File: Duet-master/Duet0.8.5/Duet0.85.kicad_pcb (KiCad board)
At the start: 4 copper layers, 100 x 123 mm, 295 parts, among them J1 EXPANSION, J10 E0 MOT/STOP, J11 E0 HEAT, J12 E0 TEMP, J13 E1 HEAT, J14 E1 TEMP, J15 uSDHC, J16 Z VREF, J17 Y VREF, J18 E0 VREF, J19 ETHERNET, J2 E1 VREF, J20 5V_PS, J21 JTAG, J22 USB, J23 POWER IN, J24 GND V_IN, J25 FAN 0 +, J26 GND, J27 GND, J28 Probe, J29 FAN 1 +, J3 X VREF, J30 PanelDUE, J31 GND V_IN, J4 BED HEAT, J5 BED TEMP, J6 E1 MOT/STOP, J7 Z MOT/STOP, J8 Y MOT/STOP, J9 X MOT/STOP, U1 ATSAM3X8E, U11 A4982SLPTR, U2 TC2117-3.3VDBTR, U3 A4403, U4 KSZ8051RNL, U5 A4982SLPTR, U6 A4982SLPTR, U7 A4982SLPTR, U8 A4982SLPTR, U9 MCP44X1, X1 CRYSTAL_4PIN, X2 CRYSTAL_4PIN

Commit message: PCB layout of components started
Experienced advice welcome.
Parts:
- removed ?: , Fixing_M4
- removed ? (x3): , Fixing_M3
- removed ?: , Duet_logo_text_conv
- removed C100, C104: 0u22, C_0603
- removed C101, C103, C105, C110, C111, C112, C93: 0u1, C_0603
- removed C102, C113, C94, C99: 100u, C_ELEC_6.3x7.7
- removed C95: 1u, C_0603
- removed C96: 22nF, C_0603
- removed C97, C98: 10u, C_0805
- removed Fid (x4): VAL**, Fiducial
- removed the J19 at (164.5, 148.4)
- removed J25: FAN 0 +, PIN_ARRAY_2X1
- removed J26, J27: GND, TP
- removed J28: Probe, PIN_ARRAY_4x1
- removed J29: FAN 1 +, PIN_ARRAY_2X1
- removed J30: PanelDUE, PIN_ARRAY_4x1
- removed J31: GND V_IN, PIN_ARRAY_2X1
- removed the J9 at (83.4, 92.1)
- removed JP10: ATX_5V_EN, JUMPER
- removed JP9: 5V_EN, JUMPER
- added C54: 10u, Melter_Connections:10mf_capacitor, F.Cu at (165.2, 70.5)
- added C6: 100u, Melter_Connections:100mf_capacitor, F.Cu at (257.4, 106.4)
- added C63: 10u, Melter_Connections:10mf_capacitor, F.Cu at (47.9, 108.5)
- added C73: 4u7, Melter_Connections:4uf7_capacitor, F.Cu at (214.4, 150.4)
- added C74: 0u1, Melter_Connections:0mf1_capacitor, F.Cu at (214.2, 148.7)
- added C79: 0u1, Melter_Connections:0mf1_capacitor, F.Cu at (217.9, 159.6)
- added C80: 10p, Melter_Connections:10pf_capacitor, F.Cu at (225.3, 159.0)
- added C81: 0u1, Melter_Connections:0mf1_capacitor, F.Cu at (217.9, 161.1)
- added C82: 0u1, Melter_Connections:0mf1_capacitor, F.Cu at (217.9, 162.6)
- added C83: 4u7, Melter_Connections:4uf7_capacitor, F.Cu at (216.8, 133.8)
- added C84: 0u1, Melter_Connections:0mf1_capacitor, F.Cu at (217.0, 132.0)
- added C85: 4u7, Melter_Connections:4uf7_capacitor, F.Cu at (223.6, 139.2)
- added C86: 0u1, Melter_Connections:0mf1_capacitor, F.Cu at (223.6, 141.0)
- added C87: 0u1, Melter_Connections:0mf1_capacitor, F.Cu at (223.6, 137.4)
- added C88: 10nF, Melter_Connections:10nf_capacitor, F.Cu at (223.6, 135.8)
- added C89: 0u1, Melter_Connections:0mf1_capacitor, F.Cu at (223.6, 134.2)
- added D22: LED0_R, Melter_Connections:LED0_diode, F.Cu at (174.4, 119.5)
- added D23: LED1_R, Melter_Connections:LED0_diode, F.Cu at (157.2, 119.9)
- added D24: LED0_B, Melter_Connections:LED0_diode, F.Cu at (174.4, 121.1)
- added D25: LED1_B, Melter_Connections:LED0_diode, F.Cu at (157.2, 121.5)
- added D26: FAN0, Melter_Connections:FAN0_diode, F.Cu at (95.8, 122.7)
- added D27: FAN1, Melter_Connections:FAN1_diode, F.Cu at (108.5, 118.8)
- added J19: USB, Melter_Connections:mUSB_new, F.Cu at (113.8, 66.5)
- added J19: USB_B, Melter_Connections:USB_Bsmd, F.Cu at (115.7, 74.9)
- added J9: 5V_PS, Melter_Connections:5VPSGND_PIN_ARRAY_3X1, F.Cu at (140.8, 134.4)
- added J9: 5V_PS, Melter_Connections:5VPSGND_PIN_ARRAY_3X1, F.Cu at (132.4, 124.6)
- added JP1: 5V_EN, Melter_Connections:JUMPER, F.Cu at (132.4, 112.4)
- added JP2: ATX_5V_EN, Melter_Connections:JUMPER, F.Cu at (132.4, 103.1)
- added K1: LED STRIP 1, Melter_Connections:USB_2, F.Cu at (173.5, 114.8)
- added K2: LED STRIP 2, Melter_Connections:USB_2, F.Cu at (156.5, 114.8)
- added K3: SENSE 1, Melter_Connections:USB_2, F.Cu at (73.5, 114.8)
- added K4: SENSE 2, Melter_Connections:USB_2, F.Cu at (56.5, 114.8)
- added R101: 4k7, Melter_Connections:4k7_R_0603, F.Cu at (108.5, 122.0)
- added R102: 100k, Melter_Connections:100k_R_0603, F.Cu at (239.2, 133.8)
- added R103: 6k8, Melter_Connections:6k8_R_0603, F.Cu at (225.3, 160.8)
- added R104: 100k, Melter_Connections:100k_R_0603, F.Cu at (232.8, 133.4)
- added R105: 100k, Melter_Connections:100k_R_0603, F.Cu at (236.0, 133.6)
- added R106: 10K, Melter_Connections:10k_R_0603, F.Cu at (235.8, 137.2)
- added R107: 10K, Melter_Connections:10k_R_0603, F.Cu at (239.0, 137.2)
- added R108: 10K, Melter_Connections:10k_R_0603, F.Cu at (233.2, 140.2)
- added R109: 10K, Melter_Connections:10k_R_0603, F.Cu at (232.8, 137.0)
- added R83: 4k7, Melter_Connections:4k7_R_0603, F.Cu at (141.1, 66.6)
- added TR10: PMV40UN2, Melter_Connections:PMV40UN2_SOT-23, F.Cu at (181.5, 109.0)
- added TR11: PMV40UN2, Melter_Connections:PMV40UN2_SOT-23, F.Cu at (165.9, 109.0)
- added TR12: PMV40UN2, Melter_Connections:PMV40UN2_SOT-23, F.Cu at (95.0, 107.3)
- added TR13: PMV40UN2, Melter_Connections:PMV40UN2_SOT-23, F.Cu at (112.3, 108.2)
- added U10: POWER/SENSE 2, Melter_Connections:USB_3, F.Cu at (107.5, 114.2)
- added U12: ATSAM3X8E, Melter_Connections:LQFP144, F.Cu at (140.2, 84.9)
- C1: value 2u2 -> 0u22; footprint C_0603 -> Melter_Connections:0mf22_capacitor
- C10: value 22u -> 0u22; footprint C_1210 -> Melter_Connections:0mf22_capacitor
- C11: value 22u -> 0u1; footprint C_1210 -> Melter_Connections:0mf1_capacitor
- C12: value 2u2 -> 0u1; footprint C_0805 -> Melter_Connections:0mf1_capacitor
- C13: value 1u -> 0u1; footprint C_0603 -> Melter_Connections:0mf1_capacitor
- C14, C17, C25, C28, C34, C35, C38, C39, C40, C41, C42, C46, C60, C64, C70, C72, C75, C78: footprint C_0603 -> Melter_Connections:0mf1_capacitor
- C15, C16, C24, C29: value 0u1 -> 0u22; footprint C_0603 -> Melter_Connections:0mf22_capacitor
- C18, C4, C7: value 10u -> 0u1; footprint C_0805 -> Melter_Connections:0mf1_capacitor
- C19: value 10u -> 100u; footprint C_0805 -> Melter_Connections:100mf_capacitor
- C2: value 0u01 -> 0u22; footprint C_0603 -> Melter_Connections:0mf22_capacitor
- C20, C31: value 0u22 -> 100u; footprint C_0603 -> Melter_Connections:100mf_capacitor
- C21, C26, C27, C30, C36, C37: value 0u22 -> 0u1; footprint C_0603 -> Melter_Connections:0mf1_capacitor
- C22, C3, C32: value 100u -> 0u1; footprint C_ELEC_6.3x7.7 -> Melter_Connections:0mf1_capacitor
- C23, C33: value 100u -> 0u22; footprint C_ELEC_6.3x7.7 -> Melter_Connections:0mf22_capacitor
- C43, C52: value 0u1 -> 1u; footprint C_0603 -> Melter_Connections:1mf_capacitor
- C44: value 10p -> 2u2; footprint C_0603 -> Melter_Connections:2mf2_capacitor
- C45: value 10p -> 100u; footprint C_0603 -> Melter_Connections:100mf_capacitor
- C47: footprint C_0805 -> Melter_Connections:10mf_capacitor
- C48: value 0u1 -> 22nF; footprint C_0603 -> Melter_Connections:22nf_capacitor
- C49, C50, C62, C69: value 0u1 -> 10u; footprint C_0603 -> Melter_Connections:10mf_capacitor
- C5, C51, C67: value 0u1 -> 100u; footprint C_0603 -> Melter_Connections:100mf_capacitor
- C53: value 10u -> 2u2; footprint C_0805 -> Melter_Connections:2mf2_capacitor
- C55, C56: value 0u1 -> 22p; footprint C_0603 -> Melter_Connections:22pf_capacitor
- C57: value 0u1 -> 22u; footprint C_0603 -> Melter_Connections:22mf_Capacitor_1210
- C58: value 2u2 -> 22u; footprint C_0805 -> Melter_Connections:22mf_Capacitor_1210
- C59: value 4u7 -> 2u2; footprint C_0805 -> Melter_Connections:2mf2_capacitor
- C61: value 4u7 -> 0u1; footprint C_0805 -> Melter_Connections:0mf1_capacitor
- C65: value 10p -> 0u1; footprint C_0603 -> Melter_Connections:0mf1_capacitor
- C66: value 4u7 -> 100u; footprint C_0805 -> Melter_Connections:100mf_capacitor
- C68: value 4u7 -> 10u; footprint C_0805 -> Melter_Connections:10mf_capacitor
- C71: value 0u1 -> 4u7; footprint C_0603 -> Melter_Connections:4uf7_capacitor
- C76, C77: value 0u1 -> 10p; footprint C_0603 -> Melter_Connections:10pf_capacitor
- C8: value 22p -> 0u1; footprint C_0603 -> Melter_Connections:0mf1_capacitor
- C9: value 22p -> 0u22; footprint C_0603 -> Melter_Connections:0mf22_capacitor
- C90: value 10nF -> 0u1; footprint C_0603 -> Melter_Connections:0mf1_capacitor
- C91: value 0.1u -> 0u1; footprint C_0603 -> Melter_Connections:0mf1_capacitor
- C92: value 100u -> 0u01; footprint C_ELEC_6.3x7.7 -> Melter_Connections:0mf01_Capacitor
- D1: value SS3P4 -> 1SS400T1G; footprint DO-220AA -> Melter_Connections:1SS400T1G
- D10: value Z Stop -> VIN; footprint D_0603 -> Melter_Connections:V_IN_Diode_0603
- D11: value E0 Stop -> 5V+; footprint D_0603 -> Melter_Connections:5V_Diode_0603
- D12: value X Stop -> 3.3V; footprint D_0603 -> Melter_Connections:33V_Diode_0603
- D13, D14: footprint uSMA -> Melter_Connections:SS14M
- D15: value VIN -> USB; footprint D_0603 -> Melter_Connections:USB_Diode_0603
- D16: value 3.3V -> TS4148; footprint D_0603 -> Melter_Connections:TS4148_Diode_0805
- D17: value 5V+ -> TS4148; footprint D_0603 -> Melter_Connections:TS4148_Diode_0805
- D18: value 1SS400T1G -> Bed Heat; footprint SOD-523 -> Melter_Connections:BED_Diode_0603
- D19: value E1 Stop -> E0 Heat; footprint D_0603 -> Melter_Connections:E0_Diode_0603
- D2: value SS3P4 -> E1 Stop; footprint DO-220AA -> Melter_Connections:E1STOP_diode
- D20: value E1 Heat -> LED0_G; footprint D_0603 -> Melter_Connections:LED0_diode
- D21: value FAN1 -> LED1_G; footprint D_0603 -> Melter_Connections:LED0_diode
- D3: value USB -> Y Stop; footprint D_0603 -> Melter_Connections:YSTOP_diode
- D4: value TS4148 -> Z Stop; footprint D_0805 -> Melter_Connections:ZSTOP_diode
- D5: value TS4148 -> E2 Stop; footprint D_0805 -> Melter_Connections:E2STOP_diode
- D6: value Bed Heat -> E0 Stop; footprint D_0603 -> Melter_Connections:E0STOP_diode
- D7: value E0 Heat -> X Stop; footprint D_0603 -> Melter_Connections:XSTOP_diode
- D8: value FAN0 -> SS3P4; footprint D_0603 -> Melter_Connections:SS3P4
- D9: value Y Stop -> SS3P4; footprint D_0603 -> Melter_Connections:SS3P4
- J1: value EXPANSION -> X VREF; footprint PIN_ARRAY_25X2 -> Melter_Connections:Vref
- J10: value E0 MOT/STOP -> GND V_IN; footprint PIN_ARRAY_7X1 -> Melter_Connections:JUMPER
- J11: value E0 HEAT -> GND V_IN; footprint PIN_ARRAY_2X1 -> Melter_Connections:JUMPER
- J12: value E0 TEMP -> E1 TEMP; footprint PIN_ARRAY_2X1 -> Melter_Connections:PIN_ARRAY_2X1
- J13: value E1 HEAT -> Probe; footprint PIN_ARRAY_2X1 -> Melter_Connections:PIN_ARRAY_4x1
- J14: value E1 TEMP -> Z STEPPER MOTOR; footprint PIN_ARRAY_2X1 -> Melter_Connections:USB_2
- J15: value uSDHC -> Y STEPPER MOTOR; footprint uSD_SKT -> Melter_Connections:USB_2
- J16: value Z VREF -> X STEPPER MOTOR; footprint Vref -> Melter_Connections:USB_2
- J17: value Y VREF -> E0 STEPPER MOTOR; footprint Vref -> Melter_Connections:USB_2
- J18: value E0 VREF -> E1 STEPPER MOTOR; footprint Vref -> Melter_Connections:USB_2
- J2: value E1 VREF -> Z VREF; footprint Vref -> Melter_Connections:Vref
- J20: value 5V_PS -> uSDHC; footprint PIN_ARRAY_3X1 -> Melter_Connections:SD_Card_Receptacle; moved to B.Cu
- J21: value JTAG -> ETHERNET; footprint MICRO_5x2 -> Melter_Connections:RJ45_MAG
- J22: value USB -> GND; footprint uUSB_new -> Melter_Connections:GND_TP
- J23: value POWER IN -> JTAG; footprint TERM_2-WAY_6.35mm -> Melter_Connections:PIN_ARRAY_5x2
- J24: value GND V_IN -> GND; footprint PIN_ARRAY_2X1 -> Melter_Connections:GND_TP
- J3: value X VREF -> Y VREF; footprint Vref -> Melter_Connections:Vref
- J4: value BED HEAT -> E0 VREF; footprint TERM_2-WAY_6.35mm -> Melter_Connections:Vref
- J5: value BED TEMP -> E1 VREF; footprint PIN_ARRAY_2X1 -> Melter_Connections:Vref
- J6: value E1 MOT/STOP -> EXPANSION; footprint PIN_ARRAY_7X1 -> Melter_Connections:PIN_ARRAY_25X2
- J7: value Z MOT/STOP -> PanelDUE; footprint PIN_ARRAY_7X1 -> Melter_Connections:PIN_ARRAY_4x1
- J8: value Y MOT/STOP -> POWER IN; footprint PIN_ARRAY_7X1 -> Melter_Connections:V_TERM_2-WAY_6.35mm
- L1: footprint L_6x6 -> Melter_Connections:10mH_L_6x6
- L2: footprint R_0603 -> Melter_Connections:FERRITE_BEAD
- L3, L4, L5, L6, L7: footprint R_0603 -> Melter_Connections:100Mhz_R_0603
- R1: value 3K3 -> 100k; footprint R_0603 -> Melter_Connections:100k_R_0603
- R10, R7, R8, R9: value 33R -> 0R1; footprint R_0603 -> Melter_Connections:0R1_R_1206
- R100: footprint R_0603 -> Melter_Connections:4k7_R_0603
- R11, R13: value 1k -> 100k; footprint R_0603 -> Melter_Connections:100k_R_0603
- R12, R14, R67: value 4k7 -> 10k; footprint R_0603 -> Melter_Connections:10k_R_0603
- R15: value 6k49 1% -> 0R; footprint R_0603 -> Melter_Connections:0R_R_0603
- R16: value 220R -> 0R; footprint R_0603 -> Melter_Connections:0R_R_0603
- R17, R20: value 220R -> 0R1; footprint R_0603 -> Melter_Connections:0R1_R_1206
- R18: value 470R -> 0R1; footprint R_0603 -> Melter_Connections:0R1_R_1206
- R19: value 4K7 -> 0R1; footprint R_0603 -> Melter_Connections:0R1_R_1206
- R2: value 39R 1% -> 10k; footprint R_0603 -> Melter_Connections:10k_R_0603
- R21: value 4K7 -> 4k7; footprint R_0603 -> Melter_Connections:4k7_R_0603
- R22: value 470R -> 100k; footprint R_0603 -> Melter_Connections:100k_R_0603
- R23: value 220R -> 10k; footprint R_0603 -> Melter_Connections:10k_R_0603
- R24, R82: value 10K -> 4k7; footprint R_0603 -> Melter_Connections:4k7_R_0603
- R25: value 100k -> 0R; footprint R_0603 -> Melter_Connections:0R_R_0603
- R26: value 100k -> 2k7; footprint R_0603 -> Melter_Connections:2k7_R_0603
- R27: value 10k -> 2K15; footprint R_0603 -> Melter_Connections:2k15_R_0603
- R28: value 100k -> 0R1; footprint R_0603 -> Melter_Connections:0R1_R_1206
- R29: value 10k -> 0R1; footprint R_0603 -> Melter_Connections:0R1_R_1206
- R3: value 39R 1% -> 100k; footprint R_0603 -> Melter_Connections:100k_R_0603
- R30: value 0R -> 10k; footprint R_0603 -> Melter_Connections:10k_R_0603
- R31: value 0R -> 100R; footprint R_0603 -> Melter_Connections:100k_R_0603
- R32, R33: value 0R1 -> 100R; footprint R_1206 -> Melter_Connections:100R_R_0603
- R34, R35: value 0R1 -> 680R; footprint R_1206 -> Melter_Connections:680R_R_0603
- R36, R40: value 100k -> 680R; footprint R_0603 -> Melter_Connections:680R_R_0603
- R37: value 2k7 -> 100R; footprint R_0603 -> Melter_Connections:100R_R_0603
- R38: value 100k -> 100R; footprint R_0603 -> Melter_Connections:100R_R_0603
- R39: value 10k -> 100R; footprint R_0603 -> Melter_Connections:100R_R_0603
- R4, R99: footprint R_0603 -> Melter_Connections:10k_R_0603
- R41: value 10k -> 680R; footprint R_0603 -> Melter_Connections:680R_R_0603
- R42: value 0R -> 680R; footprint R_0603 -> Melter_Connections:680R_R_0603
- R43: value 0R -> 100K; footprint R_0603 -> Melter_Connections:100k_R_0603
- R44, R45: footprint R_1206 -> Melter_Connections:0R1_R_1206
- R46: value 0R1 -> 2k7; footprint R_1206 -> Melter_Connections:2k7_R_0603
- R47, R93: value 0R1 -> 4k7; footprint R_1206 -> Melter_Connections:4k7_R_0603
- R48: value 6k8 -> 2K15; footprint R_0603 -> Melter_Connections:2k15_R_0603
- R49: value 100k -> 3K92; footprint R_0603 -> Melter_Connections:3k92_R_0603
- R5: value 10k -> 0R; footprint R_0603 -> Melter_Connections:0R_R_0603
- R50: value 4k7 -> 750R; footprint R_0603 -> Melter_Connections:750R_R_0603
- R51: value 4k7 -> 470R; footprint R_0603 -> Melter_Connections:470R_R_0603
- R52: value 100k -> 10K; footprint R_0603 -> Melter_Connections:10k_R_0603
- R53: value 4K7 -> 10K; footprint R_0603 -> Melter_Connections:10k_R_0603
- R54: value 2k7 -> 39R 1%; footprint R_0603 -> Melter_Connections:39_1per_R_0603
- R55: value 4k7 -> 39R 1%; footprint R_0603 -> Melter_Connections:39_1per_R_0603
- R56, R57, R59: value 100R -> 47K; footprint R_0603 -> Melter_Connections:47k_R_0603
- R58: value 100R -> 3K3; footprint R_0603 -> Melter_Connections:3k3_R_0603
- R6: value 33R -> 0R; footprint R_0603 -> Melter_Connections:0R_R_0603
- R60: value 470R -> 47K; footprint R_0603 -> Melter_Connections:47k_R_0603
- R61: value 2K15 -> 10k; footprint R_0603 -> Melter_Connections:10k_R_0603
- R62, R63, R64: value 10K -> 33R; footprint R_0603 -> Melter_Connections:33R_R_0603
- R65: value 4k7 -> 33R; footprint R_0603 -> Melter_Connections:33R_R_0603
- R66: value 10k -> 33R; footprint R_0603 -> Melter_Connections:33R_R_0603
- R68: value 4k7 -> 1k; footprint R_0603 -> Melter_Connections:1k_R_0603
- R69, R71, R96: value 680R -> 4k7; footprint R_0603 -> Melter_Connections:4k7_R_0603
- R70: value 680R -> 1k; footprint R_0603 -> Melter_Connections:1k_R_0603
- R72: value 680R -> 6k49 1%; footprint R_0603 -> Melter_Connections:6k49_1_per_R_0603
- R73, R74: value 47K -> 220R; footprint R_0603 -> Melter_Connections:220R_R_0603
- R75, R76: value 47K -> 100k; footprint R_0603 -> Melter_Connections:100k_R_0603
- R77, R78: value 100k -> 470R; footprint R_0603 -> Melter_Connections:470R_R_0603
- R79: value 470R -> 4K7; footprint R_0603 -> Melter_Connections:4k7_R_0603
- R80, R81: value 10K -> 220R; footprint R_0603 -> Melter_Connections:220R_R_0603
- R84: value 100K -> 4K7; footprint R_0603 -> Melter_Connections:4k7_R_0603
- R85: value 0R1 -> 4K7; footprint R_1206 -> Melter_Connections:4k7_R_0603
- R86, R94: value 0R1 -> 10K; footprint R_1206 -> Melter_Connections:10k_R_0603
- R87: value 3K92 -> 10K; footprint R_0603 -> Melter_Connections:10k_R_0603
- R88: value 750R -> 4k7; footprint R_0603 -> Melter_Connections:4k7_R_0603
- R89: value 100k -> 4k7; footprint R_0603 -> Melter_Connections:4k7_R_0603
- R90: value 10k -> 10K; footprint R_0603 -> Melter_Connections:10k_R_0603
- R91: value 0R -> 10K; footprint R_0603 -> Melter_Connections:10k_R_0603
- R92: value 2K15 -> 4k7; footprint R_0603 -> Melter_Connections:4k7_R_0603
- R95: value 100R -> 10K; footprint R_0603 -> Melter_Connections:10k_R_0603
- R97: value 220R -> 4k7; footprint R_0603 -> Melter_Connections:4k7_R_0603
- R98: value 4k7 -> 10K; footprint R_0603 -> Melter_Connections:10k_R_0603
- S1: value RESET -> ERASE; footprint SW_SIDE_1 -> Melter_Connections:SW_SIDE_1
- S2: value ERASE -> RESET; footprint SW_SIDE_1 -> Melter_Connections:SW_SIDE_1
- SJ1, SJ10, SJ4, SJ5, SJ8, SJ9: footprint SJ -> Melter_Connections:SJump
- SJ2, SJ6: value MS1 -> MS2; footprint SJ -> Melter_Connections:SJump
- SJ3, SJ7: value MS2 -> MS1; footprint SJ -> Melter_Connections:SJump
- TR1, TR3: footprint SOT-23 -> Melter_Connections:BSH105_SOT-23
- TR2: value IPD036N04L -> BSH105; footprint D-PAK -> Melter_Connections:BSH105_SOT-23
- TR4: footprint D-PAK -> Melter_Connections:IPD036N04L_D-PAK
- TR5: value PMV40UN2 -> IPD036N04L; footprint SOT-23 -> Melter_Connections:IPD036N04L_D-PAK
- TR6, TR7: value BSH105 -> PMV40UN2; footprint SOT-23 -> Melter_Connections:PMV40UN2_SOT-23
- TR8: value IPD036N04L -> PMV40UN2; footprint D-PAK -> Melter_Connections:PMV40UN2_SOT-23
- TR9: footprint SOT-23 -> Melter_Connections:PMV40UN2_SOT-23
- U1: value ATSAM3X8E -> A4982SLPTR; footprint LQFP144 -> Melter_Connections:A4982SPLTR_TSSOP-24-thin_pads
- U11: value A4982SLPTR -> KSZ8051RNL; footprint TSSOP-24-thin_pads -> Melter_Connections:KSZ8051RNL
- U2: value TC2117-3.3VDBTR -> A4982SLPTR; footprint SOT-223 -> Melter_Connections:A4982SPLTR_TSSOP-24-thin_pads
- U3: value A4403 -> A4982SLPTR; footprint QFN16-4x4 -> Melter_Connections:A4982SPLTR_TSSOP-24-thin_pads
- U4: value KSZ8051RNL -> A4982SLPTR; footprint QFN32-5x5 -> Melter_Connections:A4982SPLTR_TSSOP-24-thin_pads
- U5: footprint TSSOP-24-thin_pads -> Melter_Connections:A4982SPLTR_TSSOP-24-thin_pads
- U6: value A4982SLPTR -> MCP44X1; footprint TSSOP-24-thin_pads -> Melter_Connections:MCP44X1_TSSOP-20
- U7: value A4982SLPTR -> TC2117-3.3VDBTR; footprint TSSOP-24-thin_pads -> Melter_Connections:TC2117-3.3VDBTR
- U8: value A4982SLPTR -> A4403; footprint TSSOP-24-thin_pads -> Melter_Connections:A4403_QFN16-4x4
- U9: value MCP44X1 -> POWER/SENSE 1; footprint TSSOP-20 -> Melter_Connections:USB_3
- X1, X2: footprint Xtal_5x3.2 -> Melter_Connections:Xtal_5x3.2
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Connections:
- C1 pad 1: N-000009 -> Net-(C1-Pad1)
- C10 pad 1: N-00000252 -> +3.3V
- C11 pad 1: +3.3V -> Net-(C11-Pad1)
- C11 pad 2: GND -> Net-(C11-Pad2)
- C12 pad 1: N-00000264 -> Net-(C12-Pad1)
- C12 pad 2: GND -> Net-(C12-Pad2)
- C13 pad 1: VBUS -> X_REF
- C14 pad 1: X_REF -> Z_REF
- C15 pad 1: Z_REF -> Net-(C15-Pad1)
- C16 pad 1: N-00000247 -> Net-(C16-Pad1)
- C17 pad 1: N-00000262 -> GND
- C17 pad 2: GND -> V_IN
- C18 pad 1: E0_THERMISTOR -> GND
- C18 pad 2: VSSA -> V_IN
- C19 pad 1: BED_THERMISTOR -> V_IN
- C19 pad 2: VSSA -> GND
- C2 pad 1: +3.3V -> Net-(C2-Pad1)
- C2 pad 2: RESET -> GND
- C20 pad 1: N-00000191 -> V_IN
- C21 pad 1: N-00000169 -> Net-(C21-Pad1)
- C21 pad 2: GND -> V_IN
- C22 pad 1: V_IN -> Net-(C22-Pad1)
- C22 pad 2: GND -> V_IN
- C23 pad 1: V_IN -> +3.3V
- C24 pad 1: N-00000186 -> +3.3V
- C24 pad 2: V_IN -> GND
- C25 pad 1: N-00000172 -> Net-(C25-Pad1)
- C25 pad 2: V_IN -> Net-(C25-Pad2)
- C26 pad 1: +3.3V -> Net-(C26-Pad1)
- C26 pad 2: GND -> Net-(C26-Pad2)
- C27 pad 1: +3.3V -> Y_REF
- C28 pad 1: N-00000195 -> E0_REF
- C28 pad 2: N-00000190 -> GND
- C29 pad 1: N-00000196 -> Net-(C29-Pad1)
- C29 pad 2: N-00000163 -> GND
- C3 pad 1: N-000009 -> GND
- C3 pad 2: GND -> V_IN
- C30 pad 1: N-00000213 -> GND
- C30 pad 2: GND -> V_IN
- C31 pad 1: N-00000208 -> V_IN
- C32 pad 1: V_IN -> Net-(C32-Pad1)
- C32 pad 2: GND -> V_IN
- C33 pad 1: V_IN -> +3.3V
- C34 pad 1: N-00000215 -> Net-(C34-Pad1)
- C34 pad 2: V_IN -> Net-(C34-Pad2)
- C35 pad 1: N-00000209 -> +3.3V
- C35 pad 2: V_IN -> GND
- C36 pad 1: +3.3V -> E1_REF
- C37 pad 1: +3.3V -> Y_STOP
- C38 pad 1: N-00000194 -> Z_STOP
- C38 pad 2: N-00000180 -> GND
- C39 pad 1: N-00000178 -> E1_STOP
- C39 pad 2: N-00000193 -> GND
- C4 pad 1: +3.3V -> GND
- C4 pad 2: GND -> V_IN
- C40 pad 1: X_STOP -> E2_STOP
- C41 pad 1: Y_STOP -> X_STOP
- C42 pad 1: Z_STOP -> E0_STOP
- C43 pad 1: E0_STOP -> +5V
- C44 pad 1: N-0000039 -> Net-(C44-Pad1)
- C45 pad 1: N-0000026 -> Net-(C44-Pad1)
- C46 pad 1: +3.3V -> Net-(C46-Pad1)
- C48 pad 1: +3.3V -> Net-(C48-Pad1)
- C48 pad 2: GND -> Net-(C48-Pad2)
- C49 pad 1: +3.3V -> +5V
- C5 pad 1: N-000003 -> V_IN
- C50 pad 1: +3.3V -> +5V
- C51 pad 1: +3.3V -> +5V
- C52 pad 1: /Processor/VDDCORE -> VBUS
- C53 pad 1: E1_THERMISTOR -> +3.3V
- C53 pad 2: VSSA -> GND
- C55 pad 1: +3.3V -> GND
- C55 pad 2: GND -> Net-(C55-Pad2)
- C56 pad 1: Y_REF -> GND
- C56 pad 2: GND -> Net-(C56-Pad2)
- C57 pad 1: E0_REF -> Net-(C57-Pad1)
- C59 pad 1: VDDUTMI -> Net-(C59-Pad1)
- C60 pad 1: VDDUTMI -> Net-(C60-Pad1)
- C61 pad 1: VDDANA -> Net-(C61-Pad1)
- C62 pad 1: VDDANA -> E1_THERMISTOR
- C62 pad 2: GND -> VSSA
- C64 pad 1: ADVREF -> V_IN
- C65 pad 1: N-0000052 -> V_IN
- C66 pad 1: N-0000027 -> V_IN
- C67 pad 1: N-0000027 -> V_IN
- C68 pad 1: /Processor/VDDCORE -> BED_THERMISTOR
- C68 pad 2: GND -> VSSA
- C69 pad 1: /Processor/VDDCORE -> +3.3V
- C7 pad 1: N-00000253 -> Net-(C7-Pad1)
- C7 pad 2: GND -> V_IN
- C70 pad 1: /Processor/VDDCORE -> +3.3V
- C71 pad 1: /Processor/VDDCORE -> VDDUTMI
- C72 pad 1: /Processor/VDDCORE -> VDDUTMI
- C75 pad 1: GND -> ADVREF
- C75 pad 2: V_IN -> GND
- C76 pad 1: GND -> Net-(C76-Pad1)
- C76 pad 2: V_IN -> GND
- C77 pad 1: GND -> Net-(C77-Pad1)
- C77 pad 2: V_IN -> GND
- C78 pad 1: GND -> +3.3V
- C78 pad 2: V_IN -> GND
- C8 pad 1: GND -> Net-(C8-Pad1)
- C8 pad 2: N-00000257 -> V_IN
- C9 pad 1: GND -> +3.3V
- C9 pad 2: N-00000258 -> GND
- C90 pad 1: VSSA -> /Processor/VDDCORE
- C90 pad 2: N-0000079 -> GND
- C91 pad 1: V_IN -> /Processor/VDDCORE
- C92 pad 1: V_IN -> +3.3V
- C92 pad 2: GND -> RESET
- D1 pad 1: V_IN -> E1_REF
- D1 pad 2: N-000009 -> PB15/DAC0
- D10 pad 1: N-00000159 -> V_IN
- D10 pad 2: Z_STOP_CONN -> Net-(D10-Pad2)
- D11 pad 1: N-00000198 -> +5V
- D11 pad 2: E0_STOP_CONN -> Net-(D11-Pad2)
- D12 pad 1: N-00000199 -> +3.3V
- D12 pad 2: X_STOP_CONN -> Net-(D12-Pad2)
- D15 pad 1: V_IN -> VBUS
- D15 pad 2: N-0000011 -> Net-(D15-Pad2)
- D16 pad 1: +3.3V -> NRST
- D16 pad 2: N-0000010 -> Net-(C54-Pad1)
- D17 pad 1: +5V -> +3.3V
- D17 pad 2: N-0000012 -> Net-(C54-Pad1)
- D18 pad 1: E1_REF -> Net-(D18-Pad1)
- D18 pad 2: PB15/DAC0 -> BED-
- D19 pad 1: N-00000153 -> Net-(D19-Pad1)
- D19 pad 2: E1_STOP_CONN -> E0-
- D2 pad 1: N-0000014 -> Net-(D2-Pad1)
- D2 pad 2: N-0000016 -> E1_STOP_CONN
- D20 pad 1: N-00000235 -> Net-(D20-Pad1)
- D20 pad 2: E1- -> LED0_G-
- D21 pad 1: N-00000240 -> Net-(D21-Pad1)
- D21 pad 2: FAN1- -> LED1_G-
- D3 pad 1: VBUS -> Net-(D3-Pad1)
- D3 pad 2: N-00000249 -> Y_STOP_CONN
- D4 pad 1: NRST -> Net-(D4-Pad1)
- D4 pad 2: N-00000253 -> Z_STOP_CONN
- D5 pad 1: +3.3V -> Net-(D5-Pad1)
- D5 pad 2: N-00000253 -> E2_STOP_CONN
- D6 pad 1: N-00000234 -> Net-(D6-Pad1)
- D6 pad 2: BED- -> E0_STOP_CONN
- D7 pad 1: N-00000228 -> Net-(D7-Pad1)
- D7 pad 2: E0- -> X_STOP_CONN
- D8 pad 1: N-00000232 -> V_IN
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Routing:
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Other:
- board size 100 x 123 mm -> 596.5 x 234 mm
- board text removed: "*"
- board text removed: "+"
- board text removed: "+5V +3.3V TWD0 URXD PD9 TXD1 TXD0 PC29 PC28 PC7 PC23 PC21 PB24 NPCS0 MOSI PB23 AD13 TWD1 AD10 VSSA AD14 PC12 PC14 PC16 PC18"
- board text removed: "1 3 5 7 9 11 13 15 17 19 21 23 25 27 29 31 33 35 37 39 41 43 45 47 49"
- board text removed: "1B 1A 2A 2B STP 3V3 GND"
- board text removed: "2 1"
- board text removed: "2 4 6 8 10 12 14 16 18 20 22 24 26 28 30 32 34 36 38 40 42 44 46 48 50"
- board text removed: "3.3V"
- board text removed: "3.3V PC10 GND AD12"
- board text removed: "50 49"
- board text removed: "5V GND URXD UTXD"
- board text removed: "5V+"
- board text removed: "Aways On Fans"
- board text removed: "BED HEATER VIN BED-"
- board text removed: "BED TEMP"
- board text removed: "E0 HEAT"
- board text removed: "E0 Heat"
- board text removed: "E0 MOTOR/STOP"
- board text removed: "E1 HEAT"
- board text removed: "E1 Heat"
- board text removed: "E1 MOTOR/STOP"
- board text removed: "ERASE"
- board text removed: "EXPANSION HEADER"
- board text removed: "GND PS_ON 5V_IN"
- board text removed: "GND R(th)"
- board text removed: "GND RST TWCK0 UTXD PA14 RXD1 RXD0 PC30 PC4 PB14 PC22 PC20 NPCS1 SPCK MISO PB16 AD0 TWCK1 AD11 PB22 PC11 PC13 PC15 PC17 PC19"
- board text removed: "POWER IN GND VIN"
- board text removed: "PWM Fans"
- board text removed: "PanelDUE"
- board text removed: "Probe"
- board text removed: "RESET"
- board text removed: "V0.8.5 www.think3dprint3d.com/duet CERN OSH License 1.2 Design: Tony Lock, Adrian Bowyer & Andy Hingston"
- board text removed: "VIN"
- board text removed: "VIN E0 R(Th)"
- board text removed: "VIN E0-"
- board text removed: "VIN E1 R(Th)"
- board text removed: "VIN E1-"
- board text removed: "VIN FAN0-"
- board text removed: "VIN FAN1-"
- board text removed: "VIN GND"
- board text removed: "X-AXIS MOTOR/STOP"
- board text removed: "Y-AXIS MOTOR/STOP"
- board text removed: "Z-AXIS MOTOR/STOP"

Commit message: Finalising draft layout for comment
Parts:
- removed the J19 at (115.7, 74.9)
- removed the J9 at (132.4, 124.6)
- D10: value VIN -> 12V_IN
- D18: value Bed Heat -> Heat2
- D19: value E0 Heat -> Heat1
- J20: footprint Melter_Connections:SD_Card_Receptacle -> Melter_Connections:uSD_SKT; moved to F.Cu
- JP2: value ATX_5V_EN -> ATX5V_EN
- moved R105 139.3 mm to (112.2, 69.8), turned to 180 degrees
- moved R102 136.9 mm to (118.2, 69.8), turned to 180 degrees
- moved R104 133.7 mm to (115.2, 69.8), turned to 180 degrees
- moved R103 132.3 mm to (117.7, 83.8), turned to 180 degrees
- moved X2 131.0 mm to (121.3, 75.1)
- moved C76 130.8 mm to (125.3, 75.4), turned to 90 degrees
- moved C77 130.7 mm to (117.3, 75.4), turned to 90 degrees
- moved C80 129.0 mm to (119.3, 85.4), turned to 0 degrees
- moved R106 116.5 mm to (134.1, 80.3)
- moved R107 116.5 mm to (137.3, 80.3)
- moved R108 113.5 mm to (135.5, 82.5)
- moved J23 105.6 mm to (115.1, 65.8)
- moved J24 103.8 mm to (148.7, 102.0)
- moved C72 102.4 mm to (124.1, 90.2)
- moved L3 101.8 mm to (122.5, 88.6), turned to 180 degrees
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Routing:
- net GND: track 910.0 -> 1379.0 mm, vias 35 -> 65
- net Net-(J21-Pad3): track 412.0 -> 0.00 mm, vias 25 -> 0
- net (no net): track 6544.8 -> 6747.4 mm, vias 559 -> 569
- net V_IN: track 446.6 -> 300.5 mm, vias 21 -> 14
- net X_DIR: track 0.00 -> 136.2 mm, vias 0 -> 5
- net Net-(C61-Pad1): track 124.7 -> 0.00 mm, vias 4 -> 0
- net Net-(D9-Pad1): track 43.4 -> 153.0 mm, vias 1 -> 5
- net +5V: track 149.5 -> 72.2 mm, vias 2 -> 1
- net Net-(C60-Pad1): track 75.9 -> 0.00 mm, vias 6 -> 0
- net +3.3V: track 107.7 -> 183.6 mm, vias 5 -> 14
- net FAN0-: track 84.9 -> 9.08 mm, vias 3 -> 0
- net ADVREF: track 0.00 -> 68.2 mm, vias 0 -> 3
- net Net-(D25-Pad1): track 62.4 -> 0.00 mm, vias 2 -> 0
- net Net-(J21-Pad9): track 62.1 -> 0.00 mm, vias 2 -> 0
- net PS_ON_IN: track 58.6 -> 120.1 mm, vias 2 -> 5
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
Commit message: Finalising first draft layout for comment
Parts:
- D10: value 12V_IN -> V_IN
- moved D15 36.8 mm to (102.0, 78.4), turned to 180 degrees
- moved R58 34.1 mm to (103.7, 76.8), turned to 180 degrees
- moved C62 27.0 mm to (55.4, 106.2)
- moved C68 27.0 mm to (51.7, 106.2)
- moved R84 27.0 mm to (57.2, 106.4)
- moved R85 27.0 mm to (53.5, 106.4)
- moved R107 26.6 mm to (111.1, 84.7)
- moved R108 26.0 mm to (109.5, 83.1)
- moved J22 23.5 mm to (86.9, 99.6)
- moved R106 22.2 mm to (112.7, 86.3)
- moved C69 12.7 mm to (117.8, 84.1), turned to 0 degrees
- moved C70 11.7 mm to (119.6, 85.9)
- moved C39 7.20 mm to (64.2, 102.6)
- moved C42 7.20 mm to (60.0, 102.6)
- moved D2 7.20 mm to (65.8, 106.4)
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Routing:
- net GND: track 1379.0 -> 1281.8 mm, vias 65 -> 61
- net +5V: track 72.2 -> 150.4 mm, vias 1 -> 2
- net (no net): track 6747.4 -> 6782.3 mm, vias 569 -> 573
- net +3.3V: track 183.6 -> 149.3 mm, vias 14 -> 13
- net Net-(C80-Pad1): track 0.00 -> 13.6 mm
- net VDDUTMI: track 9.54 -> 15.9 mm
- net DHSDM: track 0.00 -> 3.27 mm
- net Net-(R106-Pad2): track 2.65 -> 0.00 mm
- net DFSDP: track 2.37 -> 0.00 mm
- net E1_THERMISTOR: track 1.34 -> 0.00 mm, vias 1 -> 0
- net VBUS: track 0.00 -> 1.32 mm, vias 0 -> 1
- net DFSDM: track 0.00 -> 1.30 mm
- net Net-(R108-Pad2): track 1.16 -> 0.00 mm

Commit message: USB 3 receptacles!
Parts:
- removed J14: Z STEPPER MOTOR, Melter_Connections:USB_2
- removed J15: Y STEPPER MOTOR, Melter_Connections:USB_2
- removed J16: X STEPPER MOTOR, Melter_Connections:USB_2
- removed J17: E0 STEPPER MOTOR, Melter_Connections:USB_2
- removed J18: E1 STEPPER MOTOR, Melter_Connections:USB_2
- removed K1: LED STRIP 1, Melter_Connections:USB_2
- removed K2: LED STRIP 2, Melter_Connections:USB_2
- removed K3: SENSE 1, Melter_Connections:USB_2
- removed K4: SENSE 2, Melter_Connections:USB_2
- added U13: MOTOR 5, Melter_Connections:USB_3, F.Cu at (244.5, 120.2)
- added U14: MOTOR 4, Melter_Connections:USB_3, F.Cu at (227.5, 120.2)
- added U15: MOTOR 3, Melter_Connections:USB_3, F.Cu at (210.5, 120.2)
- added U16: MOTOR 2, Melter_Connections:USB_3, F.Cu at (193.5, 120.2)
- added U17: MOTOR 1, Melter_Connections:USB_3, F.Cu at (176.5, 120.2)
- added U18: SENSE 1, Melter_Connections:USB_3, F.Cu at (59.5, 120.2)
- added U19: LED STRIP 1, Melter_Connections:USB_3, F.Cu at (159.5, 120.2)
- added U20: LED STRIP 2, Melter_Connections:USB_3, F.Cu at (142.5, 120.2)
- added U21: SENSE 2, Melter_Connections:USB_3, F.Cu at (42.5, 120.2)
- D10: value V_IN -> VIN
- D18: value Heat2 -> Bed Heat
- D19: value Heat1 -> E0 Heat
- JP2: value ATX5V_EN -> ATX_5V_EN
- moved J11 76.1 mm to (122.1, 73.3), turned to 0 degrees
- moved U7 61.2 mm to (157.0, 89.3)
- moved C47 51.7 mm to (156.9, 95.0)
- moved C43 51.1 mm to (155.3, 96.9)
- moved C83 36.8 mm to (103.8, 88.0)
- moved C84 35.0 mm to (105.6, 86.2)
- moved L7 29.4 mm to (107.2, 84.6)
- moved C62 22.0 mm to (34.4, 112.6)
- moved S2 21.2 mm to (59.4, 71.5)
- moved D1 19.6 mm to (134.6, 104.8)
- moved R27 19.6 mm to (136.0, 103.2)
- moved R106 15.5 mm to (98.9, 93.3)
- moved R107 15.5 mm to (97.3, 91.7)
- moved R108 15.5 mm to (95.7, 90.1)
- moved C60 15.4 mm to (47.3, 94.8)
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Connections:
- net E2_STOP renamed PC7_PWMH2
- net LED0_G_PWM renamed PC21_PWML4
- net LED0_R_PWM renamed PC22_PWML5
- net PC23_PWML6 renamed LED0_B_PWM
- J20 pad G: (no net) -> GND
- U10 pad 7: Net-(U10-Pad7) -> GND
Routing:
- net (no net): track 6782.3 -> 5972.0 mm, vias 573 -> 501
- net +3.3V: track 149.3 -> 522.9 mm, vias 13 -> 25
- net Net-(C48-Pad2): track 221.4 -> 5.19 mm, vias 14 -> 1
- net E0-: track 206.2 -> 22.8 mm, vias 8 -> 5
- net Net-(D12-Pad2): track 0.91 -> 160.8 mm, vias 0 -> 4
- net VDDANA: track 0.00 -> 159.8 mm, vias 0 -> 1
- net Net-(R69-Pad2): track 0.00 -> 145.0 mm, vias 0 -> 5
- net Net-(D9-Pad1): track 153.0 -> 8.94 mm, vias 5 -> 1
- net X_DIR: track 136.2 -> 0.00 mm, vias 5 -> 0
- net PS_ON_IN: track 120.1 -> 0.00 mm, vias 5 -> 0
- net BED-: track 25.1 -> 124.3 mm, vias 2 -> 32
- net PC30: track 0.00 -> 95.6 mm, vias 0 -> 2
- net LED0_G-: track 0.00 -> 86.0 mm, vias 0 -> 1
- net LED1_G-: track 38.1 -> 111.1 mm, vias 2 -> 3
- net ADVREF: track 68.2 -> 0.00 mm, vias 3 -> 0
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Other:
- board size 596.5 x 234 mm -> 286.6 x 126.9 mm
- board text added: "T0"
- board text added: "T1"
- board text added: "T2"
- board text added: "efsdfsdfsdfsdfsdfsdf"

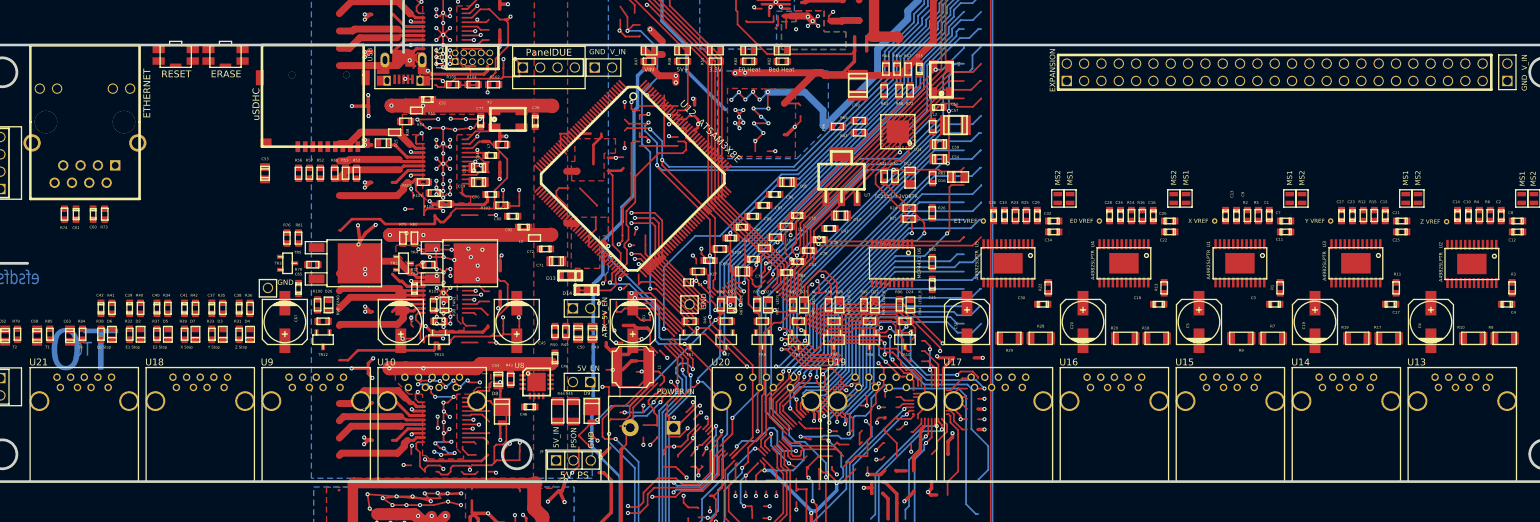
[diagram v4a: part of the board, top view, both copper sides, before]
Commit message: 0.1" headers added
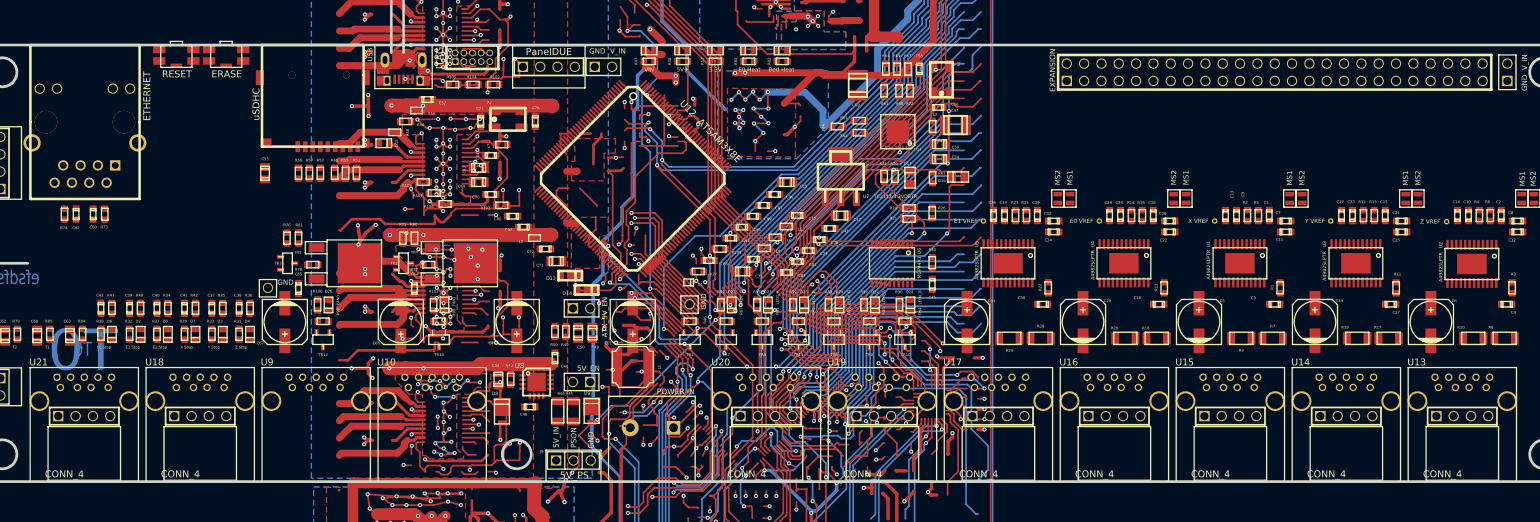
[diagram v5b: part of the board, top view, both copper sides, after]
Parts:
- added P1: CONN_4, Melter_Connections:RA_PIN_ARRAY_4x1, F.Cu at (248.0, 124.4)
- added P2: CONN_4, Melter_Connections:RA_PIN_ARRAY_4x1, F.Cu at (231.0, 124.4)
- added P3: CONN_4, Melter_Connections:RA_PIN_ARRAY_4x1, F.Cu at (214.0, 124.4)
- added P4: CONN_4, Melter_Connections:RA_PIN_ARRAY_4x1, F.Cu at (197.0, 124.4)
- added P5: CONN_4, Melter_Connections:RA_PIN_ARRAY_4x1, F.Cu at (180.0, 124.4)
- added P6: CONN_4, Melter_Connections:RA_PIN_ARRAY_4x1, F.Cu at (163.0, 124.4)
- added P7: CONN_4, Melter_Connections:RA_PIN_ARRAY_4x1, F.Cu at (146.0, 124.4)
- added P8: CONN_4, Melter_Connections:RA_PIN_ARRAY_4x1, F.Cu at (63.0, 124.4)
- added P9: CONN_4, Melter_Connections:RA_PIN_ARRAY_4x1, F.Cu at (46.0, 124.4)
- U10: value POWER/SENSE 2 -> SENSE/POWER 2
- U9: value POWER/SENSE 1 -> SENSE/POWER 1
- moved D15 0.10 mm to (89.9, 84.4)
- moved S2 0.10 mm to (59.5, 71.5)
- moved J11 0.10 mm to (122.1, 73.2)
- moved J7 0.10 mm to (114.1, 73.2)
- moved S1 0.10 mm to (66.8, 71.5)
- moved U7 0.10 mm to (156.9, 89.3)
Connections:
- net LED0_B_PWM renamed PC23_PWML6
- net LED1_R_PWM renamed PC19_PWMH5
- U10 pad 7: GND -> Net-(U10-Pad7)
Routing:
- net (no net): track 5972.0 -> 5818.5 mm, vias 501 -> 495
- net V_IN: track 234.8 -> 309.1 mm, vias 15 -> 20
- net LED1_R-: track 0.00 -> 57.0 mm, vias 0 -> 1
- net LED0_B-: track 17.5 -> 58.4 mm, vias 0 -> 1
- net LED0_R-: track 51.0 -> 41.3 mm, vias 1 -> 0
- net LED0_G-: track 86.0 -> 77.1 mm
- net Net-(U20-Pad5): track 50.0 -> 44.5 mm
- net Net-(D15-Pad2): track 10.3 -> 15.7 mm
- net PC22_PWML5: track 10.0 -> 13.4 mm, vias 1 -> 2
- net Net-(U19-Pad5): track 6.65 -> 3.22 mm, vias 1 -> 0

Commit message: Routing started
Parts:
- added REF**: MountingHole_3mm, Mounting_Holes:MountingHole_3mm, F.Cu at (262.5, 55.8)
- added REF**: MountingHole_3mm, Mounting_Holes:MountingHole_3mm, F.Cu at (262.5, 111.8)
- added REF**: MountingHole_3mm, Mounting_Holes:MountingHole_3mm, F.Cu at (111.9, 111.8)
- added REF**: MountingHole_3mm, Mounting_Holes:MountingHole_3mm, F.Cu at (36.5, 111.8)
- added REF**: MountingHole_3mm, Mounting_Holes:MountingHole_3mm, F.Cu at (36.5, 55.8)
- J10: value GND V_IN -> GND V_IN
- U10: value SENSE/POWER 2 -> USB_3.0_Receptacle
- U13: value MOTOR 5 -> USB_3.0_Receptacle_4
- U14: value MOTOR 4 -> USB_3.0_Receptacle_4
- U15: value MOTOR 3 -> USB_3.0_Receptacle_4
- U16: value MOTOR 2 -> USB_3.0_Receptacle_4
- U17: value MOTOR 1 -> USB_3.0_Receptacle_4
- U18: value SENSE 1 -> USB_3.0_Receptacle_3
- U19: value LED STRIP 1 -> USB_3.0_Receptacle_2
- U20: value LED STRIP 2 -> USB_3.0_Receptacle_2
- U21: value SENSE 2 -> USB_3.0_Receptacle_3
- U9: value SENSE/POWER 1 -> USB_3.0_Receptacle
- moved C56 23.9 mm to (170.9, 55.3), turned to 90 degrees
- moved JP1 21.7 mm to (121.1, 97.8)
- moved R44 21.2 mm to (119.2, 102.8)
- moved R45 21.2 mm to (121.5, 102.8)
- moved D9 21.2 mm to (124.1, 102.1)
- moved X2 20.0 mm to (114.0, 61.8)
- moved C76 20.0 mm to (118.0, 62.1)
- moved C77 20.0 mm to (109.9, 62.1), turned to 270 degrees
- moved D8 19.8 mm to (109.7, 103.4)
- moved R40 19.3 mm to (60.8, 90.4)
- moved C52 19.0 mm to (98.8, 59.1)
- moved R43 19.0 mm to (110.4, 100.1)
- moved C44 19.0 mm to (108.6, 100.1), turned to 270 degrees
- moved R55 19.0 mm to (97.2, 60.8)
- moved R54 18.9 mm to (95.6, 62.5)
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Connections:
- net E1_STOP renamed E1_PWM
- net PC21_PWML4 renamed LED0_G_PWM
- net PC23_PWML6 renamed LED0_B_PWM
- U10 pad 7: Net-(U10-Pad7) -> GND
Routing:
- net (no net): track 5818.5 -> 0.00 mm, vias 495 -> 0
- net GND: track 1243.9 -> 616.4 mm, vias 68 -> 0
- net +3.3V: track 522.9 -> 137.5 mm, vias 25 -> 0
- net V_IN: track 309.1 -> 688.7 mm, vias 20 -> 0
- net +5V: track 206.9 -> 38.0 mm, vias 9 -> 0
- net VSSA: track 0.00 -> 160.1 mm, vias 0 -> 4
- net Net-(D12-Pad2): track 160.8 -> 1.60 mm, vias 4 -> 0
- net VDDANA: track 159.8 -> 6.00 mm, vias 1 -> 0
- net Net-(R69-Pad2): track 145.0 -> 6.24 mm, vias 5 -> 0
- net PC30: track 95.6 -> 0.00 mm, vias 2 -> 0
- net LED1_G-: track 111.1 -> 21.1 mm, vias 3 -> 0
- net E0_THERMISTOR: track 0.00 -> 76.1 mm, vias 0 -> 2
- net PS_ON_CONTROL: track 75.1 -> 1.71 mm, vias 1 -> 0
- net BED-: track 124.3 -> 65.1 mm, vias 32 -> 0
- net LED0_G-: track 77.1 -> 21.9 mm, vias 1 -> 0
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- removed copper zone on B.Cu, net +3.3V
- removed copper zone on F.Cu, net +3.3V
- removed copper zone on Inner3, net +3.3V
- removed copper zone on B.Cu, net BED-
- removed copper zone on F.Cu, net BED-
- removed copper zone on B.Cu, net E0-
- removed copper zone on F.Cu, net E0-
- removed copper zone on B.Cu, net E1-
- removed copper zone on F.Cu, net E1-
- removed copper zone on F.Cu, net FAN0-
- removed copper zone on F.Cu, net FAN1-
- removed copper zone on B.Cu, net GND
- removed copper zone on F.Cu, net GND
- removed copper zone on Inner2, net GND
- removed copper zone on B.Cu, net N-0000016
- removed copper zone on F.Cu, net N-0000016
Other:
- board size 286.6 x 126.9 mm -> 286.6 x 277.8 mm
- net class 0.500 added: clearance 0.254, trace_width 0.44, via_dia 0.8001, via_drill 0.5
- board text removed: "efsdfsdfsdfsdfsdfsdf"
- board text removed: "www.think3dprint3d.com/duet"
